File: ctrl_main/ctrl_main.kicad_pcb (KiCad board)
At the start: 2 copper layers, 53.3 x 101.6 mm, 19 parts, among them IC1 SN74HC125N, J1 B2B-XH-A(LF)(SN), J2 B2B-XH-A(LF)(SN), J3 B2B-XH-A(LF)(SN), P10 CONN_01X04, P11 CONN_01X03, P12 CONN_01X03, P4 CONN_01X04, P5 CONN_01X04, P6 CONN_01X04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

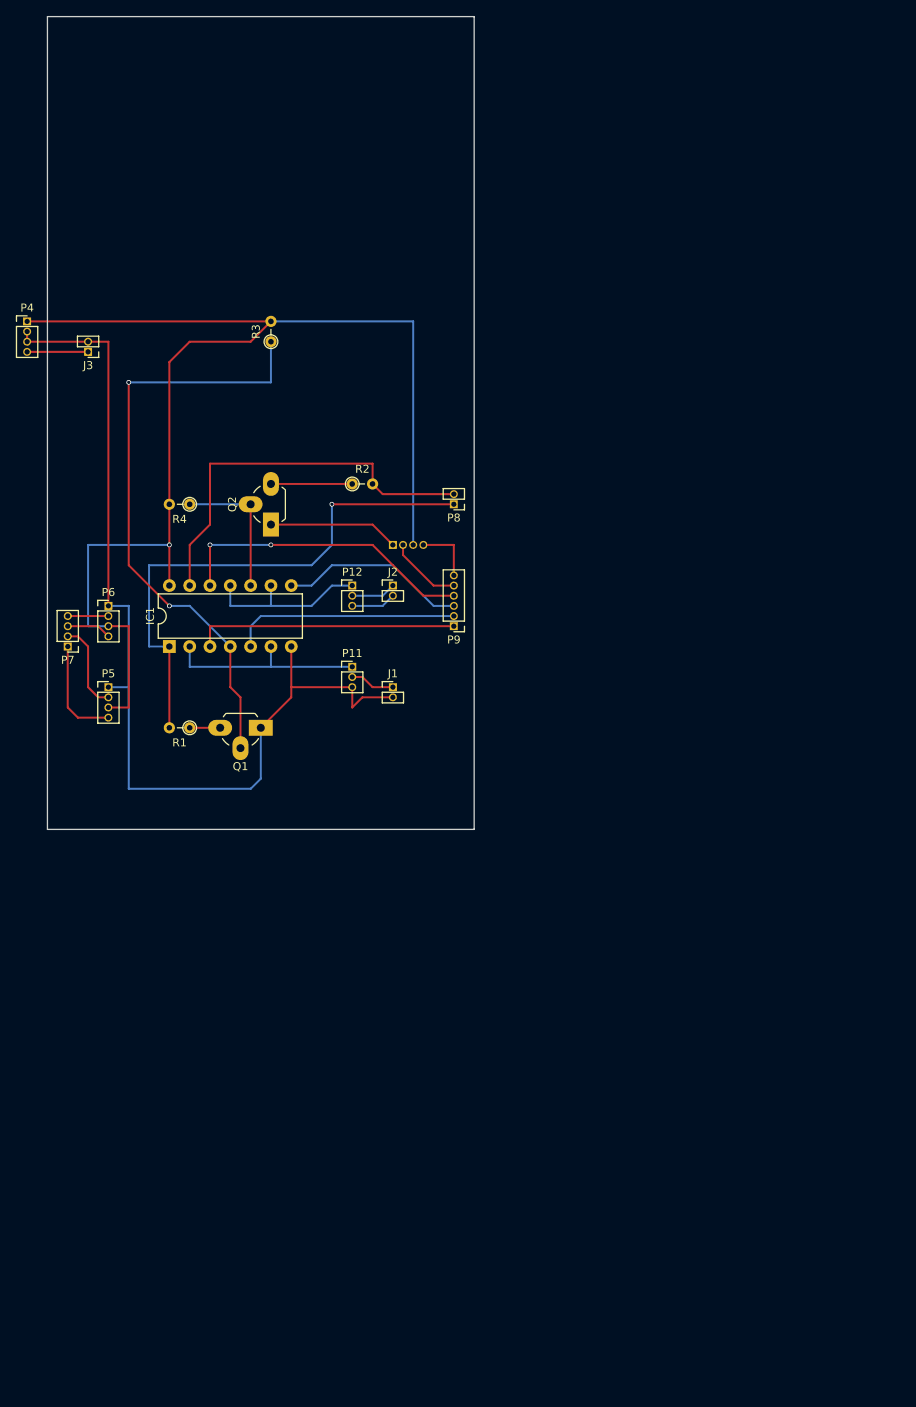
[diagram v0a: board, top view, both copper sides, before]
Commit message: CTRL7V4->Vin Rev2.1
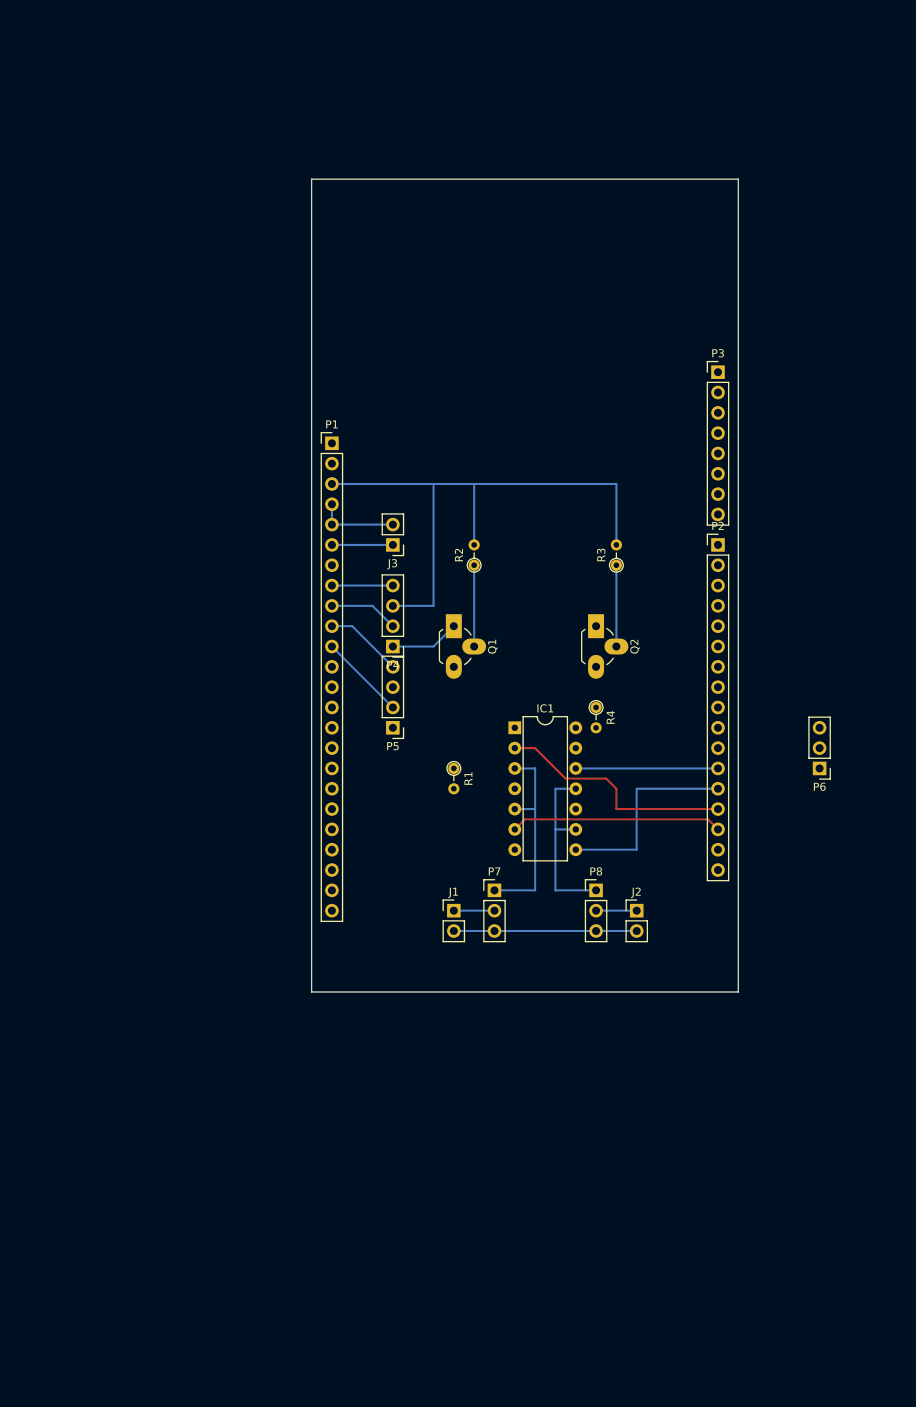
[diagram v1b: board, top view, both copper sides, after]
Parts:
- removed P10: CONN_01X04, Pin_Headers:Pin_Header_Straight_1x04_Pitch1.27mm
- removed P11, P12: CONN_01X03, Pin_Headers:Pin_Header_Straight_1x03_Pitch1.27mm
- removed P9: CONN_01X06, Pin_Headers:Pin_Header_Straight_1x06_Pitch1.27mm
- added P1: ANALOG, Pin_Headers:Pin_Header_Straight_1x24_Pitch2.54mm, F.Cu at (201.9, 76.2)
- added P2: DIGITAL_L, Pin_Headers:Pin_Header_Straight_1x17_Pitch2.54mm, F.Cu at (250.2, 88.9)
- added P3: DIGITAL_H, Pin_Headers:Pin_Header_Straight_1x08_Pitch2.54mm, F.Cu at (250.2, 67.3)
- J1, J2, J3: footprint Pin_Headers:Pin_Header_Straight_1x02_Pitch1.27mm -> Pin_Headers:Pin_Header_Straight_1x02_Pitch2.54mm
- P4: value CONN_01X04 -> JS_H; footprint Pin_Headers:Pin_Header_Straight_1x04_Pitch1.27mm -> Pin_Headers:Pin_Header_Straight_1x04_Pitch2.54mm
- P5: value CONN_01X04 -> JS_V; footprint Pin_Headers:Pin_Header_Straight_1x04_Pitch1.27mm -> Pin_Headers:Pin_Header_Straight_1x04_Pitch2.54mm
- P6: value CONN_01X04 -> SDC; footprint Pin_Headers:Pin_Header_Straight_1x04_Pitch1.27mm -> Pin_Headers:Pin_Header_Straight_1x03_Pitch2.54mm
- P7: value CONN_01X04 -> SVH; footprint Pin_Headers:Pin_Header_Straight_1x04_Pitch1.27mm -> Pin_Headers:Pin_Header_Straight_1x03_Pitch2.54mm
- P8: value CONN_01X02 -> SVV; footprint Pin_Headers:Pin_Header_Straight_1x02_Pitch1.27mm -> Pin_Headers:Pin_Header_Straight_1x03_Pitch2.54mm
- moved P6 91.2 mm to (262.9, 116.8), turned to 180 degrees
- moved P7 61.4 mm to (222.2, 132.1), turned to 0 degrees
- moved P4 61.2 mm to (209.6, 101.6), turned to 180 degrees
- moved R4 56.8 mm to (234.9, 109.2), turned to 270 degrees
- moved P8 51.4 mm to (234.9, 132.1), turned to 0 degrees
- moved R3 51.4 mm to (237.5, 91.4)
- moved J2 50.8 mm to (240.0, 134.6)
- moved J3 45.1 mm to (209.6, 88.9)
- moved IC1 44.4 mm to (224.8, 111.8), turned to 0 degrees
- moved Q2 42.6 mm to (234.9, 99.1), turned to 270 degrees
- moved P5 35.9 mm to (209.6, 111.8), turned to 180 degrees
- moved R1 33.4 mm to (217.2, 116.8), turned to 270 degrees
- moved J1 29.0 mm to (217.2, 134.6)
- moved Q1 27.3 mm to (217.2, 99.1), turned to 270 degrees
- moved R2 18.3 mm to (219.7, 91.4), turned to 90 degrees
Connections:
- IC1 pad 10: Net-(IC1-Pad10) -> D3
- IC1 pad 12: Net-(IC1-Pad12) -> TX2
- IC1 pad 2: Net-(IC1-Pad2) -> TX1
- IC1 pad 4: Net-(IC1-Pad4) -> D2
- IC1 pad 5: Net-(IC1-Pad5) -> Net-(IC1-Pad3)
- IC1 pad 6: Net-(IC1-Pad2) -> RX1
- IC1 pad 8: Net-(IC1-Pad8) -> RX2
- J3 pad 1: CTRL7V4 -> Vin
- P4 pad 1: 5V -> CTRLGND
- P4 pad 2: CTRLGND -> A1
- P4 pad 3: CTRLGND -> 5V
- P4 pad 4: CTRL7V4 -> A0
- P5 pad 2: Net-(P5-Pad2) -> A3
- P5 pad 4: Net-(P5-Pad4) -> A2
- P6 pad 2: Net-(P6-Pad2) -> RX3
- P6 pad 3: 5V -> TX3
- P7 pad 1: Net-(P5-Pad4) -> Net-(IC1-Pad3)
- P7 pad 2: Net-(P5-Pad2) -> SVH11V1
- P7 pad 3: Net-(P6-Pad4) -> CTRLGND
- P8 pad 1: Net-(IC1-Pad1) -> Net-(IC1-Pad11)
- P8 pad 2: Net-(IC1-Pad13) -> SVV11V1
- Q1 pad 2: Net-(IC1-Pad4) -> Net-(IC1-Pad1)
- Q2 pad 2: Net-(IC1-Pad10) -> Net-(IC1-Pad13)
- R1 pad 2: Net-(IC1-Pad1) -> D2
- R2 pad 1: Net-(Q2-Pad3) -> Net-(IC1-Pad1)
- R2 pad 2: Net-(IC1-Pad13) -> 5V
- R3 pad 1: Net-(IC1-Pad4) -> Net-(IC1-Pad13)
- R4 pad 1: Net-(IC1-Pad10) -> Net-(Q2-Pad3)
- R4 pad 2: 5V -> D3
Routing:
- net CTRLGND: track 145.2 -> 41.7 mm
- net 5V: track 157.0 -> 71.1 mm, vias 1 -> 0
- net Net-(IC1-Pad4): track 75.9 -> 0.00 mm, vias 2 -> 0
- net Net-(IC1-Pad1): track 67.1 -> 10.2 mm, vias 1 -> 0
- net Net-(IC1-Pad13): track 49.8 -> 10.2 mm
- net Net-(IC1-Pad12): track 38.2 -> 0.00 mm, vias 2 -> 0
- net TX1: track 0.00 -> 30.0 mm
- net Net-(IC1-Pad5): track 28.5 -> 0.00 mm
- net RX1: track 0.00 -> 26.5 mm
- net RX2: track 0.00 -> 25.4 mm
- net Net-(IC1-Pad2): track 25.4 -> 0.00 mm
- net Net-(IC1-Pad8): track 23.5 -> 0.00 mm
- net Net-(IC1-Pad10): track 17.8 -> 0.00 mm
- net TX2: track 0.00 -> 17.8 mm
- net Net-(P5-Pad4): track 13.2 -> 0.00 mm
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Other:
- board text added: "Hole Area"

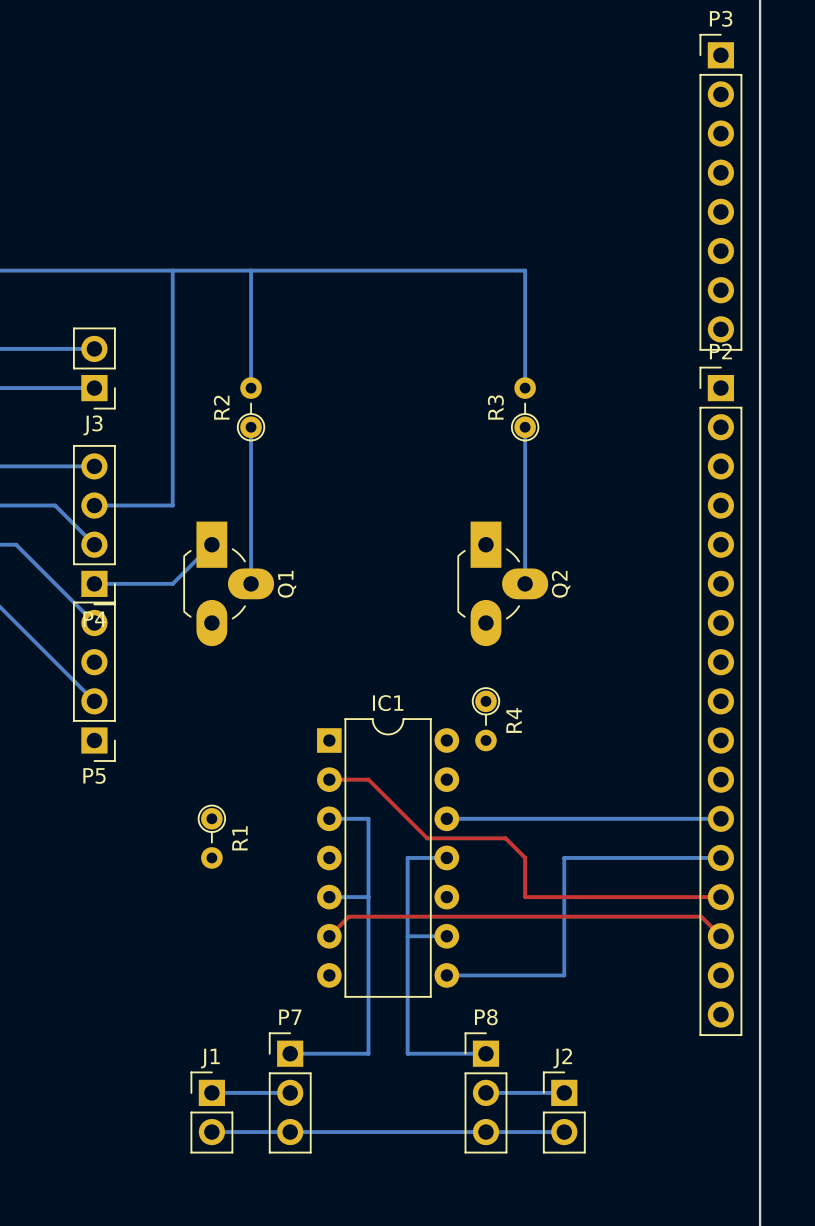
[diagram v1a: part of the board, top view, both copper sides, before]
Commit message: フットプリントの配置と配線
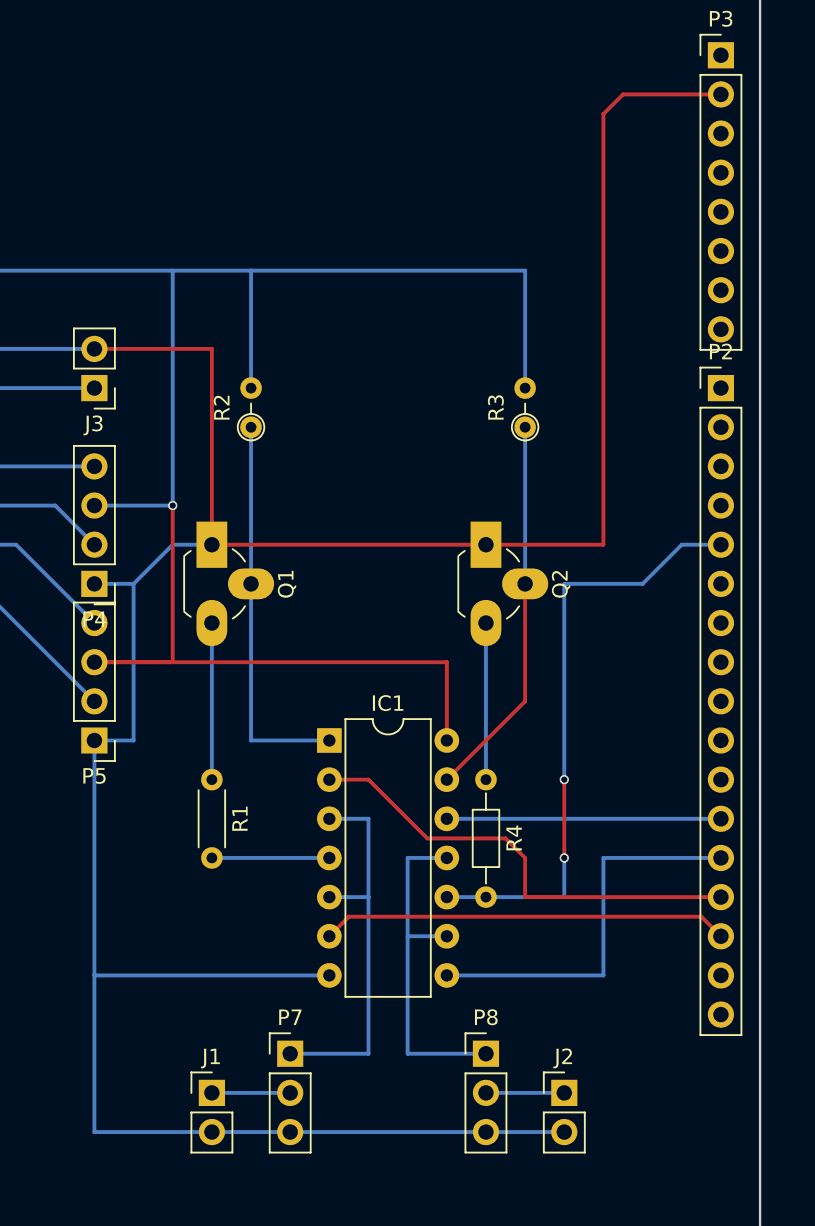
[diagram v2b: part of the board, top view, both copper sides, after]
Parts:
- R1: footprint Resistors_ThroughHole:R_Axial_DIN0204_L3.6mm_D1.6mm_P2.54mm_Vertical -> Resistors_ThroughHole:R_Axial_DIN0204_L3.6mm_D1.6mm_P5.08mm_Horizontal
- R4: footprint Resistors_ThroughHole:R_Axial_DIN0204_L3.6mm_D1.6mm_P2.54mm_Vertical -> Resistors_ThroughHole:R_Axial_DIN0204_L3.6mm_D1.6mm_P7.62mm_Horizontal
- moved R4 5.08 mm to (234.9, 114.3)
- moved R1 2.54 mm to (217.2, 114.3)
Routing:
- net CTRLGND: track 41.7 -> 184.5 mm
- net 5V: track 71.1 -> 114.3 mm, vias 0 -> 1
- net D3: track 0.00 -> 39.2 mm, vias 0 -> 2
- net Net-(IC1-Pad1): track 10.2 -> 25.4 mm
- net Net-(IC1-Pad13): track 10.2 -> 25.0 mm
- net Net-(Q2-Pad3): track 0.00 -> 10.2 mm
- net Net-(Q1-Pad3): track 0.00 -> 10.2 mm
- net D2: track 0.00 -> 7.62 mm

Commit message: P6のRXとTX入れ替え。フットプリントの配置と配線完了
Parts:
- moved P6 21.7 mm to (242.6, 109.2), turned to 0 degrees
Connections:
- P6 pad 2: RX3 -> TX3
- P6 pad 3: TX3 -> RX3
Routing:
- net CTRLGND: track 184.5 -> 194.6 mm
- net TX3: track 0.00 -> 7.62 mm
- net RX3: track 0.00 -> 7.62 mm
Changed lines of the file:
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@@
   (general
     (links 45)
-    (no_connects 4)
+    (no_connects 1)
     (area 199.314999 43.104999 252.805001 144.855001)
     (thickness 1.6)
     (drawings 19)
-    (tracks 84)
+    (tracks 87)
     (zones 0)
     (modules 18)
@@
   )
   (module Pin_Headers:Pin_Header_Straight_1x03_Pitch2.54mm (layer F.Cu)
-    (at 262.89 116.84 180)
+    (at 242.57 109.22)
     (descr "Through hole straight pin header, 1x03, 2.54mm pitch, single row")
     (tags "Through hole pin header THT 1x03 2.54mm single row")
-    (fp_text reference P6 (at 0 -2.33 180) (layer F.SilkS)
-      (effects (font (size 1 1) (thickness 0.15)))
-    )
-    (fp_text value SDC (at 0 7.41 180) (layer F.Fab)
+    (fp_text reference P6 (at 0 -2.33) (layer F.SilkS)
+      (effects (font (size 1 1) (thickness 0.15)))
+    )
+    (fp_text value SDC (at 0 7.41) (layer F.Fab)
       (effects (font (size 1 1) (thickness 0.15)))
     )
@@
     (fp_line (start 1.8 6.85) (end 1.8 -1.8) (layer F.CrtYd) (width 0.05))
     (fp_line (start 1.8 -1.8) (end -1.8 -1.8) (layer F.CrtYd) (width 0.05))
-    (fp_text user %R (at 0 -2.33 180) (layer F.Fab)
-      (effects (font (size 1 1) (thickness 0.15)))
-    )
-    (pad 1 thru_hole rect (at 0 0 180) (size 1.7 1.7) (drill 1) (layers *.Cu *.Mask)
-      (net 2 CTRLGND))
-    (pad 2 thru_hole oval (at 0 2.54 180) (size 1.7 1.7) (drill 1) (layers *.Cu *.Mask)
+    (fp_text user %R (at 0 -2.33) (layer F.Fab)
+      (effects (font (size 1 1) (thickness 0.15)))
+    )
+    (pad 1 thru_hole rect (at 0 0) (size 1.7 1.7) (drill 1) (layers *.Cu *.Mask)
+      (net 2 CTRLGND))
+    (pad 2 thru_hole oval (at 0 2.54) (size 1.7 1.7) (drill 1) (layers *.Cu *.Mask)
+      (net 45 TX3))
+    (pad 3 thru_hole oval (at 0 5.08) (size 1.7 1.7) (drill 1) (layers *.Cu *.Mask)
       (net 46 RX3))
-    (pad 3 thru_hole oval (at 0 5.08 180) (size 1.7 1.7) (drill 1) (layers *.Cu *.Mask)
-      (net 45 TX3))
     (model ${KISYS3DMOD}/Pin_Headers.3dshapes/Pin_Header_Straight_1x03_Pitch2.54mm.wrl
       (at (xyz 0 -0.1 0))
@@
   )
   (segment (start 217.17 134.62) (end 222.25 134.62) (width 0.25) (layer B.Cu) (net 1))
-  (segment (start 217.17 137.16) (end 209.55 137.16) (width 0.25) (layer B.Cu) (net 2) (status 400000))
+  (segment (start 242.57 109.22) (end 242.57 99.06) (width 0.25) (layer F.Cu) (net 2) (status 400000))
+  (segment (start 217.17 137.16) (end 209.55 137.16) (width 0.25) (layer B.Cu) (net 2))
   (segment (start 209.55 137.16) (end 209.55 127) (width 0.25) (layer B.Cu) (net 2))
   (segment (start 234.95 99.06) (end 242.57 99.06) (width 0.25) (layer F.Cu) (net 2))
@@
   (segment (start 217.17 114.3) (end 217.17 104.14) (width 0.25) (layer B.Cu) (net 9))
   (segment (start 234.95 114.3) (end 234.95 104.14) (width 0.25) (layer B.Cu) (net 10) (status 10))
-  (segment (start 250.19 119.38) (end 242.57 119.38) (width 0.25) (layer B.Cu) (net 11) (status 400000))
-  (segment (start 242.57 127) (end 232.41 127) (width 0.25) (layer B.Cu) (net 11) (status 800000))
+  (segment (start 250.19 119.38) (end 242.57 119.38) (width 0.25) (layer B.Cu) (net 11))
+  (segment (start 242.57 127) (end 232.41 127) (width 0.25) (layer B.Cu) (net 11))
   (segment (start 242.57 119.38) (end 242.57 127) (width 0.25) (layer B.Cu) (net 11))
   (segment (start 250.19 121.92) (end 237.49 121.92) (width 0.25) (layer F.Cu) (net 12))
@@
   (segment (start 237.49 119.38) (end 236.22 118.11) (width 0.25) (layer F.Cu) (net 12))
   (segment (start 237.49 121.92) (end 237.49 119.38) (width 0.25) (layer F.Cu) (net 12))
-  (segment (start 234.95 121.92) (end 240.03 121.92) (width 0.25) (layer B.Cu) (net 13) (status 400000))
-  (segment (start 247.65 99.06) (end 250.19 99.06) (width 0.25) (layer B.Cu) (net 13) (status 800000))
+  (segment (start 234.95 121.92) (end 240.03 121.92) (width 0.25) (layer B.Cu) (net 13))
+  (segment (start 247.65 99.06) (end 250.19 99.06) (width 0.25) (layer B.Cu) (net 13))
   (segment (start 245.11 101.6) (end 247.65 99.06) (width 0.25) (layer B.Cu) (net 13))
   (segment (start 240.03 101.6) (end 245.11 101.6) (width 0.25) (layer B.Cu) (net 13))
@@
   (via (at 240.03 119.38) (size 0.6) (drill 0.4) (layers F.Cu B.Cu) (net 13))
   (segment (start 240.03 121.92) (end 240.03 119.38) (width 0.25) (layer B.Cu) (net 13))
-  (segment (start 232.41 121.92) (end 234.95 121.92) (width 0.25) (layer B.Cu) (net 13) (status C00000))
+  (segment (start 232.41 121.92) (end 234.95 121.92) (width 0.25) (layer B.Cu) (net 13))
   (segment (start 224.79 119.38) (end 217.17 119.38) (width 0.25) (layer B.Cu) (net 14))
   (segment (start 250.19 116.84) (end 232.41 116.84) (width 0.25) (layer B.Cu) (net 15))
@@
   (segment (start 204.47 99.06) (end 209.55 104.14) (width 0.25) (layer B.Cu) (net 23))
   (segment (start 201.93 101.6) (end 209.55 109.22) (width 0.25) (layer B.Cu) (net 24))
+  (segment (start 250.19 111.76) (end 242.57 111.76) (width 0.25) (layer B.Cu) (net 45) (status C00000))
+  (segment (start 242.57 114.3) (end 250.19 114.3) (width 0.25) (layer B.Cu) (net 46) (status C00000))
 )

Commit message: フットプリントに図名等入れた
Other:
- board text added: "2.2"
- board text added: "2017/05/02"
- board text added: "Servo ctrl."
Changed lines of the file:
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@@
     (area 199.314999 43.104999 252.805001 144.855001)
     (thickness 1.6)
-    (drawings 19)
+    (drawings 22)
     (tracks 87)
     (zones 0)
@@
     )
   )
+  (gr_text "Servo ctrl." (at 194.31 190.5) (layer F.Cu)
+    (effects (font (size 1.5 1.5) (thickness 0.3)))
+  )
+  (gr_text 2.2 (at 270.51 193.04) (layer F.Cu)
+    (effects (font (size 1.5 1.5) (thickness 0.3)))
+  )
+  (gr_text 2017/05/02 (at 214.63 193.04) (layer F.Cu)
+    (effects (font (size 1.5 1.5) (thickness 0.3)))
+  )
   (gr_text "Hole Area" (at 209.55 48.26) (layer Dwgs.User)

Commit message: update schs
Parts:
- moved P8 11.4 mm to (229.9, 121.9)
- moved IC1 10.5 mm to (222.2, 101.6)
- moved J1 10.5 mm to (214.6, 124.5)
- moved J2 10.5 mm to (237.5, 124.5)
- moved P7 10.2 mm to (222.2, 121.9)
- moved R1 10.2 mm to (217.2, 104.1)
- moved R4 10.2 mm to (234.9, 104.1)
- moved Q1 7.62 mm to (217.2, 91.4)
- moved Q2 7.62 mm to (234.9, 91.4)
- moved R2 7.62 mm to (219.7, 83.8)
- moved R3 7.62 mm to (237.5, 83.8)
- moved P5 2.54 mm to (209.6, 114.3)
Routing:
- net TX1: track 30.0 -> 0.00 mm
- net RX1: track 26.5 -> 0.00 mm
- net 5V: track 114.3 -> 95.0 mm, vias 1 -> 2
- net TX2: track 17.8 -> 0.00 mm
- net CTRLGND: track 194.6 -> 185.9 mm
- net D3: track 39.2 -> 33.0 mm, vias 2 -> 0
- net Net-(IC1-Pad1): track 25.4 -> 20.3 mm
- net RX2: track 25.4 -> 21.4 mm
- net A3: track 10.8 -> 14.8 mm
- net Net-(IC1-Pad3): track 25.4 -> 22.9 mm
- net Net-(IC1-Pad11): track 22.9 -> 20.3 mm
- net A2: track 9.72 -> 12.3 mm
- net SVV11V1: track 5.08 -> 7.62 mm
- net SVH11V1: track 5.08 -> 7.62 mm
- net Net-(Q2-Pad3): track 10.2 -> 7.62 mm
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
